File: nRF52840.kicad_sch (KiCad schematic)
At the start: 20 parts, among them J3 JTAG_TC2030, J4 RGB, Q2 2N7002, Q3 AO3407, SW29 RESET, U4 MS88SF3

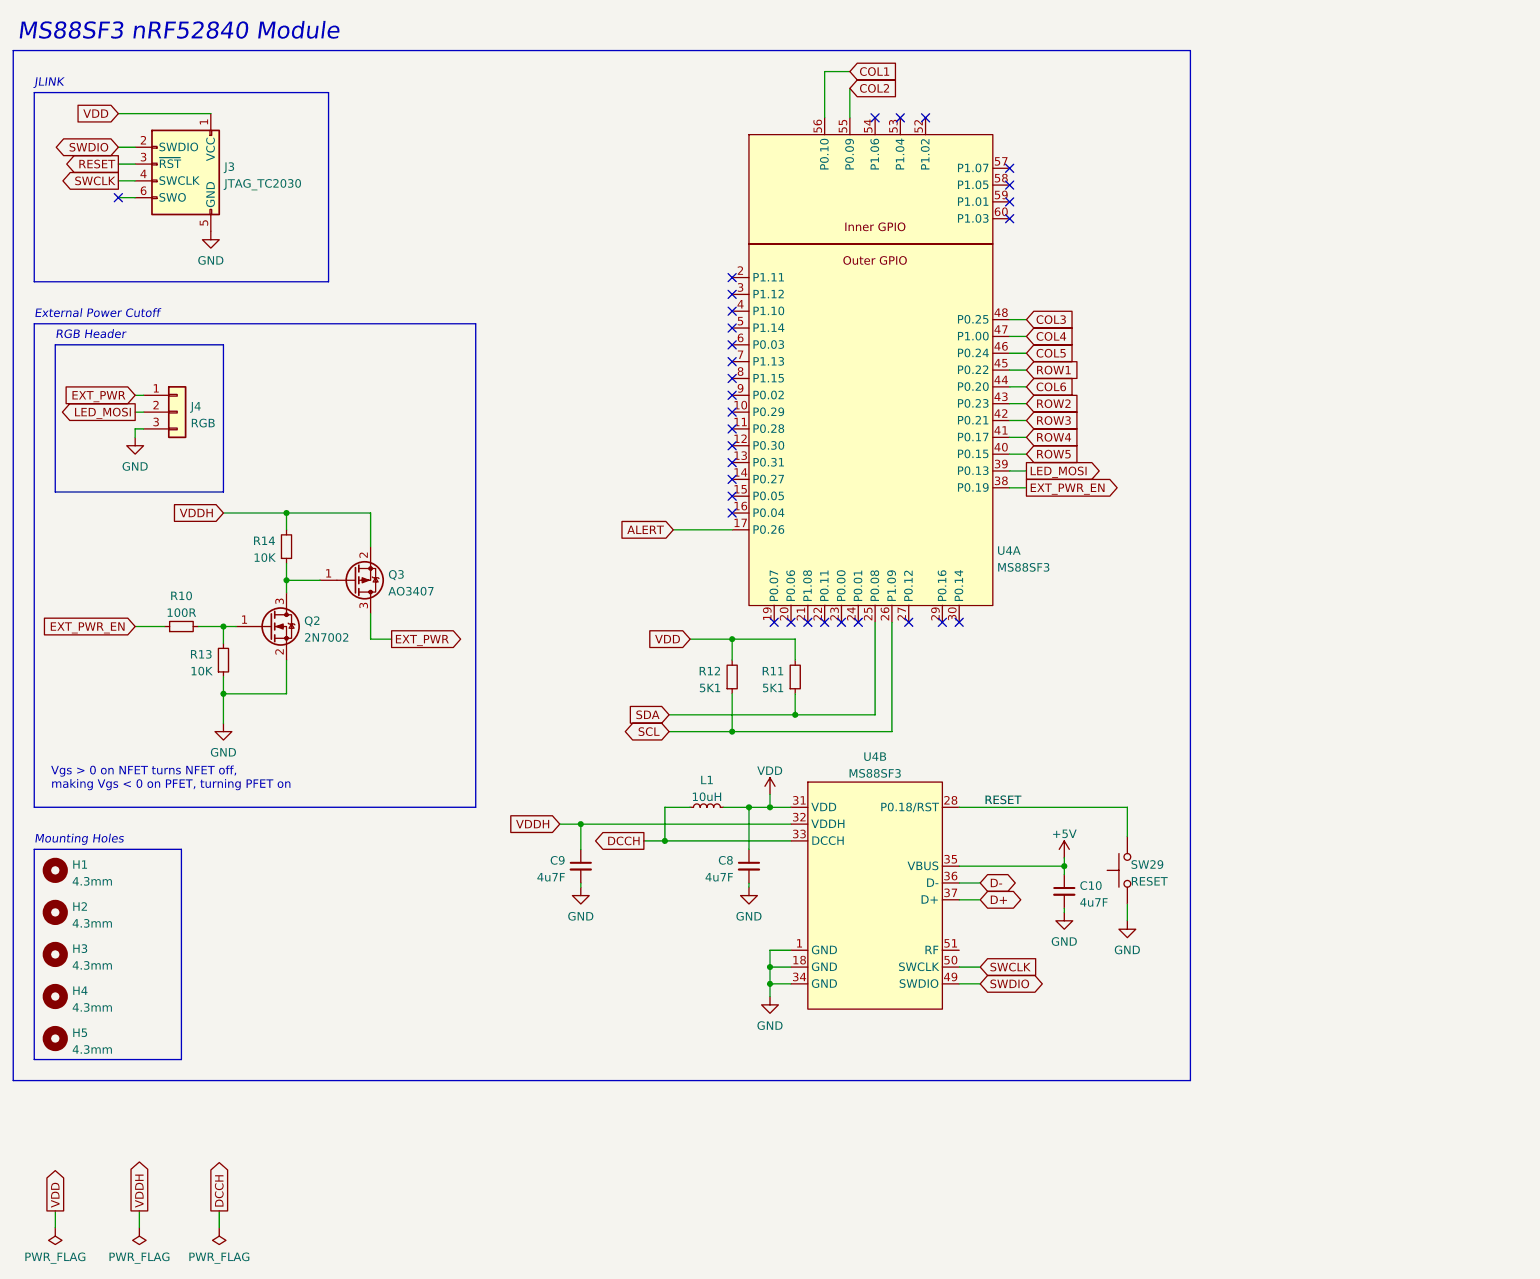
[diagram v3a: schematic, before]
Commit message: feat(pcb): Version 0.4
- Prepare to move from JLC7628 stackup to JLC3313 stackup (Lowers dielectric constant from 4.6 to 4.05)
- Increase mounting hole diameter back to 5.4mm
- 6mil signals, 10mil power, 13 mil vias
  - 3W spacing wherever possible
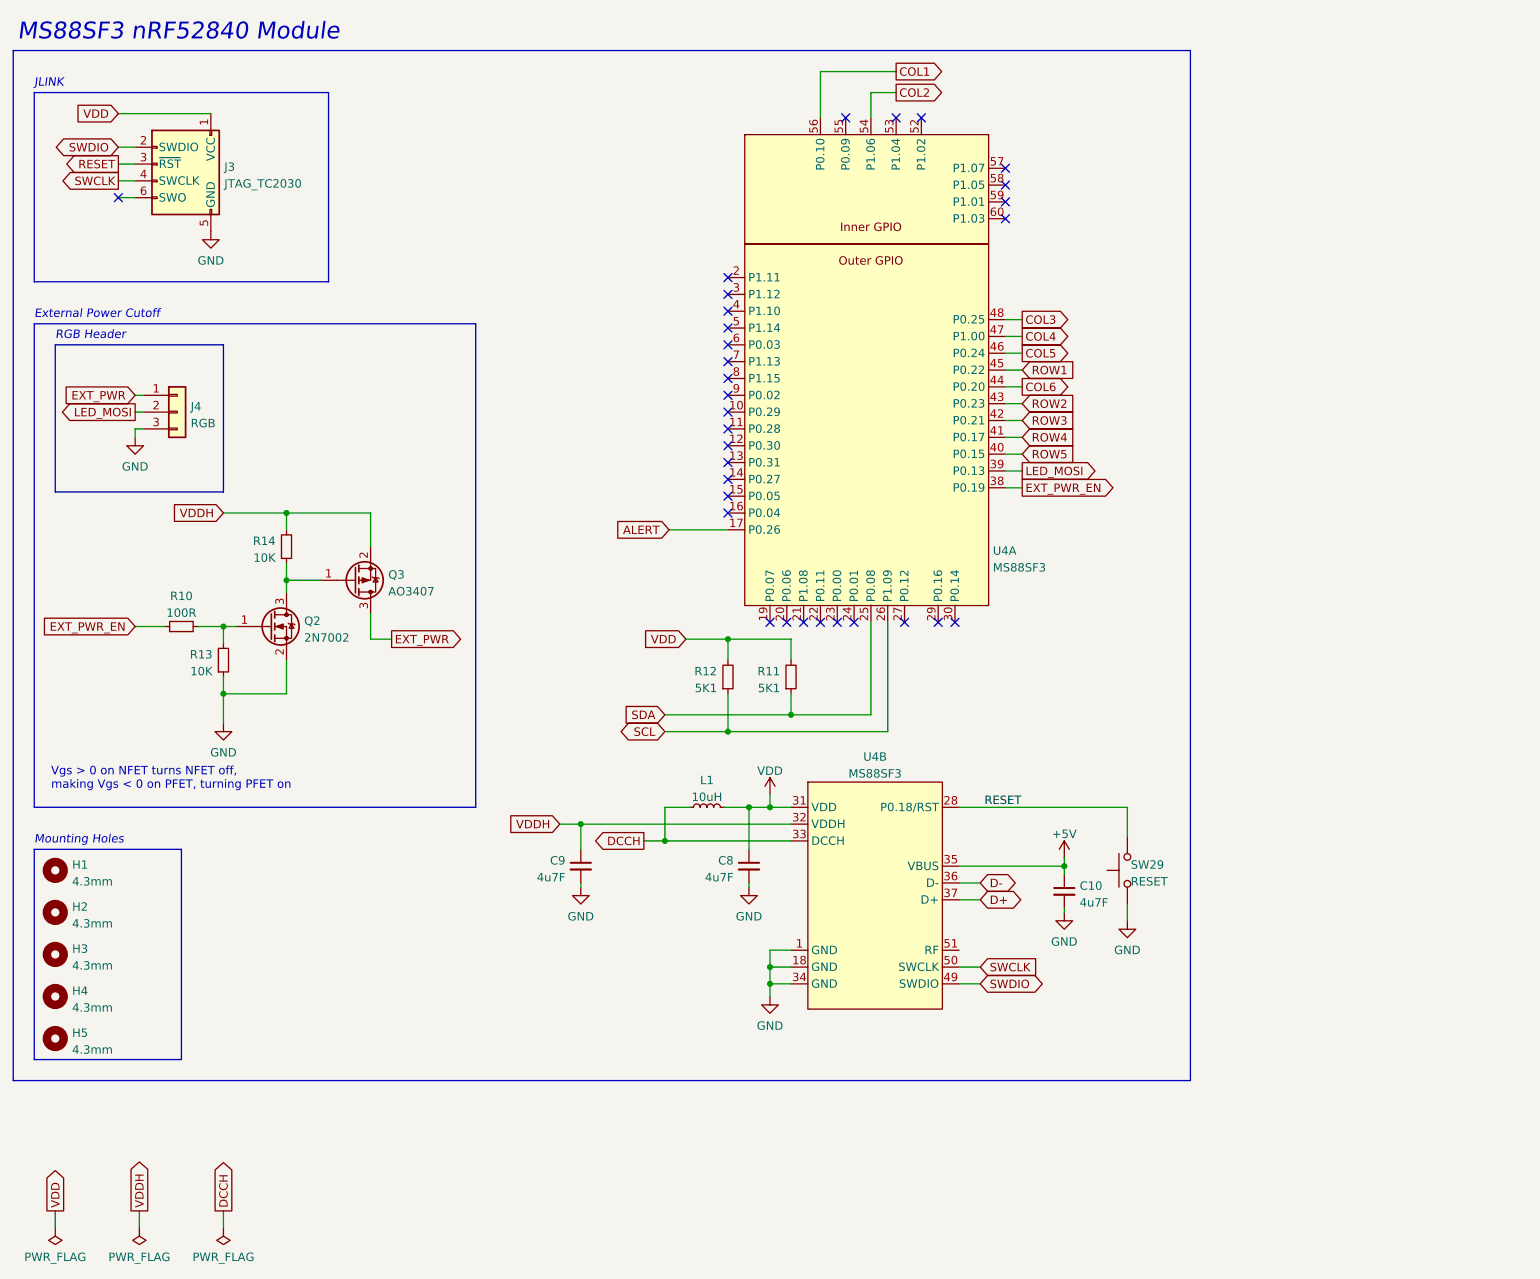
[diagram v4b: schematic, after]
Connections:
- net COL2: now also U4.54 (P1.06); no longer U4.55 (P0.09)
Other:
- moved on the sheet: R11, R12, U4A

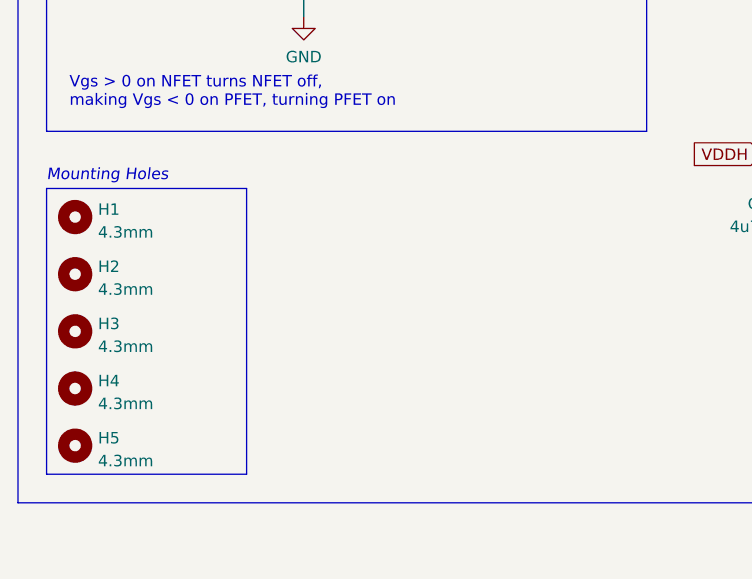
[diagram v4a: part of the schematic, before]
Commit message: feat(pcb): Version 0.4.1
- Add oscilloscope probing pads/labels
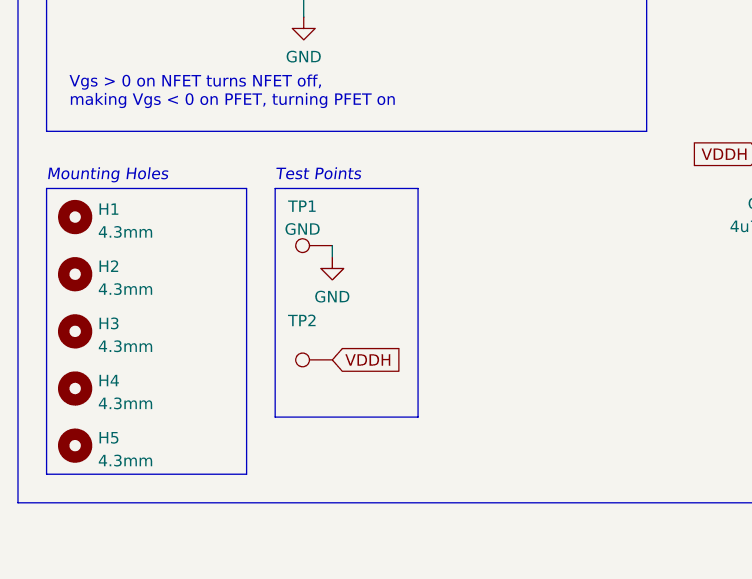
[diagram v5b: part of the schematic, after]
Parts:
- added TP1: GND, TestPoint:TestPoint_THTPad_1.0x1.0mm_Drill0.5mm, symbol Connector:TestPoint
- added TP2: (no value), symbol Connector:TestPoint
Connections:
- net GND: now also TP1.1
- net VDDH: now also TP2.1
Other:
- note added: "Test Points"
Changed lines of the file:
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@@
+    (stroke (width 0) (type default) (color 0 0 0 0))
+  )
+  (polyline (pts (xy 41.275 139.7) (xy 41.275 165.1))
     (stroke (width 0) (type default) (color 0 0 0 0))
   )
@@
     (stroke (width 0) (type default) (color 0 0 0 0))
   )
+  (polyline (pts (xy 41.275 165.1) (xy 57.15 165.1))
+    (stroke (width 0) (type default) (color 0 0 0 0))
+  )
   (wire (pts (xy 130.175 135.89) (xy 98.425 135.89))
     (stroke (width 0) (type default) (color 0 0 0 0))
@@
     (stroke (width 0) (type default) (color 0 0 0 0))
   )
+  (polyline (pts (xy 57.15 139.7) (xy 41.275 139.7))
+    (stroke (width 0) (type default) (color 0 0 0 0))
+  )
   (wire (pts (xy 120.015 133.35) (xy 123.825 133.35))
     (stroke (width 0) (type default) (color 0 0 0 0))
@@
     (stroke (width 0) (type default) (color 0 0 0 0))
   )
+  (polyline (pts (xy 57.15 165.1) (xy 57.15 139.7))
+    (stroke (width 0) (type default) (color 0 0 0 0))
+  )
   (wire (pts (xy 53.975 99.06) (xy 59.055 99.06))
     (stroke (width 0) (type default) (color 0 0 0 0))
@@
     (stroke (width 0) (type default) (color 0 0 0 0))
   )
+  (wire (pts (xy 47.625 147.32) (xy 47.625 146.05))
+    (stroke (width 0) (type default) (color 0 0 0 0))
+  )
   (wire (pts (xy 44.45 88.9) (xy 53.975 88.9))
     (stroke (width 0) (type default) (color 0 0 0 0))
@@
   (wire (pts (xy 28.575 36.195) (xy 31.115 36.195))
     (stroke (width 0) (type default) (color 0 0 0 0))
+  )
+  (text "Test Points" (at 41.275 139.065 0)
+    (effects (font (size 1.27 1.27) italic) (justify left bottom))
   )
   (text "RGB Header" (at 19.05 62.865 0)
@@
     (effects (font (size 1.27 1.27)) (justify left))
     (property "Intersheet References" "${INTERSHEET_REFS}" (id 0) (at 31.6706 186.9379 90)
+      (effects (font (size 1.27 1.27)) (justify left) hide)
+    )
+  )
+  (global_label "VDDH" (shape input) (at 47.625 158.75 0) (fields_autoplaced)
+    (effects (font (size 1.27 1.27)) (justify left))
+    (property "Intersheet References" "${INTERSHEET_REFS}" (id 0) (at 54.9971 158.8294 0)
       (effects (font (size 1.27 1.27)) (justify left) hide)
     )
@@
     )
   )
+  (symbol (lib_id "Connector:TestPoint") (at 47.625 158.75 90) (unit 1)
+    (in_bom yes) (on_board yes) (fields_autoplaced)
+    (property "Reference" "TP2" (id 0) (at 44.323 154.4152 90))
+    (property "Value" "" (id 1) (at 44.323 156.9521 90))
+    (property "Footprint" "" (id 2) (at 47.625 153.67 0)
+      (effects (font (size 1.27 1.27)) hide)
+    )
+    (property "Datasheet" "~" (id 3) (at 47.625 153.67 0)
+      (effects (font (size 1.27 1.27)) hide)
+    )
+    (pin "1")
+  )
   (symbol (lib_id "power:GND") (at 123.825 145.415 0) (unit 1)
     (in_bom yes) (on_board yes)
@@
       (effects (font (size 1.27 1.27)) hide)
     )
+    (pin "1")
+  )
+  (symbol (lib_id "Connector:TestPoint") (at 47.625 146.05 90) (unit 1)
+    (in_bom yes) (on_board yes) (fields_autoplaced)
+    (property "Reference" "TP1" (id 0) (at 44.323 141.7152 90))
+    (property "Value" "GND" (id 1) (at 44.323 144.2521 90))
+    (property "Footprint" "TestPoint:TestPoint_THTPad_1.0x1.0mm_Drill0.5mm" (id 2) (at 47.625 140.97 0)
+      (effects (font (size 1.27 1.27)) hide)
+    )
+    (property "Datasheet" "~" (id 3) (at 47.625 140.97 0)
+      (effects (font (size 1.27 1.27)) hide)
+    )
+    (pin "1")
+  )
+  (symbol (lib_id "power:GND") (at 47.625 147.32 0) (unit 1)
+    (in_bom yes) (on_board yes) (fields_autoplaced)
+    (property "Reference" "#PWR0128" (id 0) (at 47.625 153.67 0)
+      (effects (font (size 1.27 1.27)) hide)
+    )
+    (property "Value" "GND" (id 1) (at 47.625 151.7634 0))
+    (property "Footprint" "" (id 2) (at 47.625 147.32 0)
+      (effects (font (size 1.27 1.27)) hide)
+    )
+    (property "Datasheet" "" (id 3) (at 47.625 147.32 0)
+      (effects (font (size 1.27 1.27)) hide)
+    )
